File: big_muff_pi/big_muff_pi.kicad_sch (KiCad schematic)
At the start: 77 parts, among them J1 Jack_6.35, J2 Jack_6.35, J6 top_panel_connector, J7 Conn_01x01_Socket, J8 Conn_01x01_Socket, J9 Barrel_Jack_Switch, P1 front_panel, P2 bottom_panel, Q1 MMBT5551, Q10 AO3401A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

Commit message: small mods.
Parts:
- removed SIM1: Logo_Open_Hardware_Small, Symbol:OSHW-Logo2_7.3x6mm_SilkScreen, symbol Graphic:Logo_Open_Hardware_Small
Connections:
- net 0: now also J6.16 (Pin_16); no longer J6.6 (Pin_6)
- net FS_OUT: now also J6.2 (Pin_2); no longer J6.12 (Pin_12)
- net at J6.4 (Pin_4): now also R7.1; no longer SW1.3 (C)
- net at C11.2: now also J6.12 (Pin_12); no longer J6.2 (Pin_2)
- net at J6.14 (Pin_14): now also SW1.3 (C); no longer R7.1
- net at R6.1: now also J6.6 (Pin_6); no longer J6.16 (Pin_16)
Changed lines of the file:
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@@
 	)
 	(symbol
+		(lib_id "pedale:top_panel_connector")
+		(at 134.62 54.61 0)
+		(unit 1)
+		(exclude_from_sim no)
+		(in_bom yes)
+		(on_board yes)
+		(dnp no)
+		(property "Reference" "J6"
+			(at 135.636 46.228 0)
+			(effects
+				(font
+					(size 1.27 1.27)
+				)
+				(hide yes)
+			)
+		)
+		(property "Value" "top_panel_connector"
+			(at 137.16 59.69 0)
+			(effects
+				(font
+					(size 1.27 1.27)
+				)
+				(hide yes)
+			)
+		)
+		(property "Footprint" "Connector_IDC:IDC-Header_2x08_P2.54mm_Vertical"
+			(at 134.62 54.61 0)
+			(effects
+				(font
+					(size 1.27 1.27)
+				)
+				(hide yes)
+			)
+		)
+		(property "Datasheet" "~"
+			(at 134.62 54.61 0)
+			(effects
+				(font
+					(size 1.27 1.27)
+				)
+				(hide yes)
+			)
+		)
+		(property "Description" ""
+			(at 120.65 94.234 0)
+			(effects
+				(font
+					(size 1.27 1.27)
+				)
+				(hide yes)
+			)
+		)
+		(pin "8"
+		)
+		(pin "11"
+		)
+		(pin "13"
+		)
+		(pin "9"
+		)
+		(pin "16"
+		)
+		(pin "14"
+		)
+		(pin "15"
+		)
+		(pin "1"
+		)
+		(pin "10"
+		)
+		(pin "3"
+		)
+		(pin "7"
+		)
+		(pin "2"
+		)
+		(pin "5"
+		)
+		(pin "4"
+		)
+		(pin "6"
+		)
+		(pin "12"
+		)
+		(instances
+			(project "big_muff_pi"
+				(path "/1fda0e48-ac05-4486-b24b-352a2425b266"
+					(reference "J6")
+					(unit 1)
+				)
+			)
+		)
+	)
+	(symbol
 		(lib_id "Simulation_SPICE:0")
 		(at 54.61 143.51 0)
@@
 	)
 	(symbol
-		(lib_id "Graphic:Logo_Open_Hardware_Small")
-		(at 77.47 91.44 0)
-		(unit 1)
-		(exclude_from_sim no)
-		(in_bom yes)
-		(on_board yes)
-		(dnp no)
-		(fields_autoplaced yes)
-		(property "Reference" "SIM1"
-			(at 77.47 84.455 0)
-			(effects
-				(font
-					(size 1.27 1.27)
-				)
-				(hide yes)
-			)
-		)
-		(property "Value" "Logo_Open_Hardware_Small"
-			(at 77.47 97.155 0)
-			(effects
-				(font
-					(size 1.27 1.27)
-				)
-				(hide yes)
-			)
-		)
-		(property "Footprint" "Symbol:OSHW-Logo2_7.3x6mm_SilkScreen"
-			(at 77.47 91.44 0)
-			(effects
-				(font
-					(size 1.27 1.27)
-				)
-				(hide yes)
-			)
-		)
-		(property "Datasheet" "~"
-			(at 77.47 91.44 0)
-			(effects
-				(font
-					(size 1.27 1.27)
-				)
-				(hide yes)
-			)
-		)
-		(property "Description" "Open Hardware logo, small"
-			(at 77.47 91.44 0)
-			(effects
-				(font
-					(size 1.27 1.27)
-				)
-				(hide yes)
-			)
-		)
-		(instances
-			(project ""
-				(path "/1fda0e48-ac05-4486-b24b-352a2425b266"
-					(reference "SIM1")
-					(unit 1)
-				)
-			)
-		)
-	)
-	(symbol
 		(lib_id "Device:R")
 		(at 130.81 167.64 0)
@@
 	)
 	(symbol
-		(lib_id "pedale:top_panel_connector")
-		(at 172.72 125.73 0)
-		(unit 1)
-		(exclude_from_sim no)
-		(in_bom yes)
-		(on_board yes)
-		(dnp no)
-		(property "Reference" "J6"
-			(at 173.736 117.348 0)
-			(effects
-				(font
-					(size 1.27 1.27)
-				)
-				(hide yes)
-			)
-		)
-		(property "Value" "top_panel_connector"
-			(at 175.26 130.81 0)
-			(effects
-				(font
-					(size 1.27 1.27)
-				)
-				(hide yes)
-			)
-		)
-		(property "Footprint" "Connector_IDC:IDC-Header_2x08_P2.54mm_Vertical"
-			(at 172.72 125.73 0)
-			(effects
-				(font
-					(size 1.27 1.27)
-				)
-				(hide yes)
-			)
-		)
-		(property "Datasheet" "~"
-			(at 172.72 125.73 0)
-			(effects
-				(font
-					(size 1.27 1.27)
-				)
-				(hide yes)
-			)
-		)
-		(property "Description" ""
-			(at 158.75 165.354 0)
-			(effects
-				(font
-					(size 1.27 1.27)
-				)
-				(hide yes)
-			)
-		)
-		(pin "8"
-		)
-		(pin "11"
-		)
-		(pin "13"
-		)
-		(pin "9"
-		)
-		(pin "16"
-		)
-		(pin "14"
-		)
-		(pin "15"
-		)
-		(pin "1"
-		)
-		(pin "10"
-		)
-		(pin "3"
-		)
-		(pin "7"
-		)
-		(pin "2"
-		)
-		(pin "5"
-		)
-		(pin "4"
-		)
-		(pin "6"
-		)
-		(pin "12"
-		)
-		(instances
-			(project "big_muff_pi"
-				(path "/1fda0e48-ac05-4486-b24b-352a2425b266"
-					(reference "J6")
-					(unit 1)
-				)
-			)
-		)
-	)
-	(symbol
-		(lib_id "pedale:top_panel_connector")
-		(at 134.62 54.61 0)
-		(unit 3)
-		(exclude_from_sim no)
-		(in_bom yes)
-		(on_board yes)
-		(dnp no)
-		(fields_autoplaced yes)
-		(property "Reference" "J6"
-			(at 135.636 46.228 0)
-			(effects
-				(font
-					(size 1.27 1.27)
-				)
-				(hide yes)
-			)
-		)
-		(property "Value" "top_panel_connector"
-			(at 137.16 59.69 0)
-			(effects
-				(font
-					(size 1.27 1.27)
-				)
-				(hide yes)
-			)
-		)
-		(property "Footprint" "Connector_IDC:IDC-Header_2x08_P2.54mm_Vertical"
-			(at 134.62 54.61 0)
-			(effects
-				(font
-					(size 1.27 1.27)
-				)
-				(hide yes)
-			)
-		)
-		(property "Datasheet" "~"
-			(at 134.62 54.61 0)
-			(effects
-				(font
-					(size 1.27 1.27)
-				)
-				(hide yes)
-			)
-		)
-		(property "Description" ""
-			(at 120.65 94.234 0)
-			(effects
-				(font
-					(size 1.27 1.27)
-				)
-				(hide yes)
-			)
-		)
-		(pin "8"
-		)
-		(pin "11"
-		)
-		(pin "13"
-		)
-		(pin "9"
-		)
-		(pin "16"
-		)
-		(pin "14"
-		)
-		(pin "15"
-		)
-		(pin "1"
-		)
-		(pin "10"
-		)
-		(pin "3"
-		)
-		(pin "7"
-		)
-		(pin "2"
-		)
-		(pin "5"
-		)
-		(pin "4"
-		)
-		(pin "6"
-		)
-		(pin "12"
-		)
-		(instances
-			(project "big_muff_pi"
-				(path "/1fda0e48-ac05-4486-b24b-352a2425b266"
-					(reference "J6")
-					(unit 3)
-				)
-			)
-		)
-	)
-	(symbol
 		(lib_id "Transistor_BJT:BC817")
 		(at 229.87 55.88 0)
@@
 				)
 			)
+		)
+	)
+	(symbol
+		(lib_id "pedale:top_panel_connector")
+		(at 172.72 125.73 0)
+		(unit 3)
+		(exclude_from_sim no)
+		(in_bom yes)
+		(on_board yes)
+		(dnp no)
+		(property "Reference" "J6"
+			(at 173.736 117.348 0)
+			(effects
+				(font
+					(size 1.27 1.27)
+				)
+				(hide yes)
+			)
+		)
+		(property "Value" "top_panel_connector"
+			(at 175.26 130.81 0)
+			(effects
+				(font
+					(size 1.27 1.27)
+				)
+				(hide yes)
+			)
+		)
+		(property "Footprint" "Connector_IDC:IDC-Header_2x08_P2.54mm_Vertical"
+			(at 172.72 125.73 0)
+			(effects
+				(font
+					(size 1.27 1.27)
+				)
+				(hide yes)
+			)
+		)
+		(property "Datasheet" "~"
+			(at 172.72 125.73 0)
+			(effects
+				(font
+					(size 1.27 1.27)
+				)
+				(hide yes)
+			)
+		)
+		(property "Description" ""
+			(at 158.75 165.354 0)
+			(effects
+				(font
+					(size 1.27 1.27)
+				)
+				(hide yes)
+			)
+		)
+		(pin "8"
+		)
+		(pin "11"
+		)
+		(pin "13"
+		)
+		(pin "9"
+		)
+		(pin "16"
+		)
+		(pin "14"
+		)
+		(pin "15"
+		)
+		(pin "1"
+		)
+		(pin "10"
+		)
+		(pin "3"
+		)
+		(pin "7"
+		)
+		(pin "2"
+		)
+		(pin "5"
+		)
+		(pin "4"
+		)
+		(pin "6"
+		)
+		(pin "12"
+		)
+		(instances
+			(project "big_muff_pi"
+				(path "/1fda0e48-ac05-4486-b24b-352a2425b266"
+					(reference "J6")
+					(unit 3)
+				)
+			)

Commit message: New switch, fixed courtyards.
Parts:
- SW1: footprint pedale:foot_switch_tht_and_floating -> pedale:foot_switch_tht_no_pad
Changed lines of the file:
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@@
 			)
 		)
-		(property "Footprint" "pedale:foot_switch_tht_and_floating"
+		(property "Footprint" "pedale:foot_switch_tht_no_pad"
 			(at 260.35 114.3 0)
 			(effects
@@
 			)
 		)
-		(property "Footprint" "pedale:foot_switch_tht_and_floating"
+		(property "Footprint" "pedale:foot_switch_tht_no_pad"
 			(at 204.47 128.27 0)
 			(effects

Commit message: Main board almost ready.
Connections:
- no-connect marks 4 -> 11
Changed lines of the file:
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@@
+	)
+	(no_connect
+		(at 30.48 54.61)
+	)
+	(no_connect
+		(at 218.44 125.73)
 	)
 	(no_connect
@@
 	)
 	(no_connect
+		(at 218.44 135.89)
+	)
+	(no_connect
 		(at 182.88 154.94)
+	)
+	(no_connect
+		(at 30.48 57.15)
 	)
 	(no_connect
@@
 		(at 182.88 160.02)
 	)
+	(no_connect
+		(at 30.48 49.53)
+	)
+	(no_connect
+		(at 218.44 130.81)
+	)
+	(no_connect
+		(at 218.44 133.35)
+	)
 	(wire

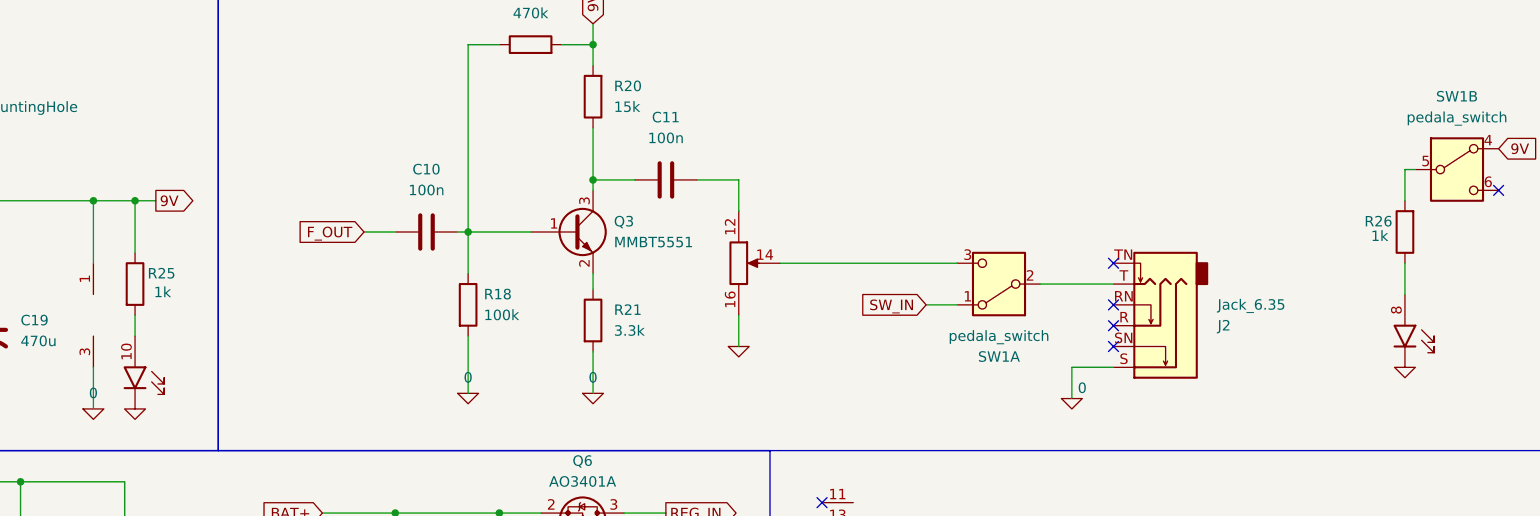
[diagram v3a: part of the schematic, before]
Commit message: 2.2k LED.
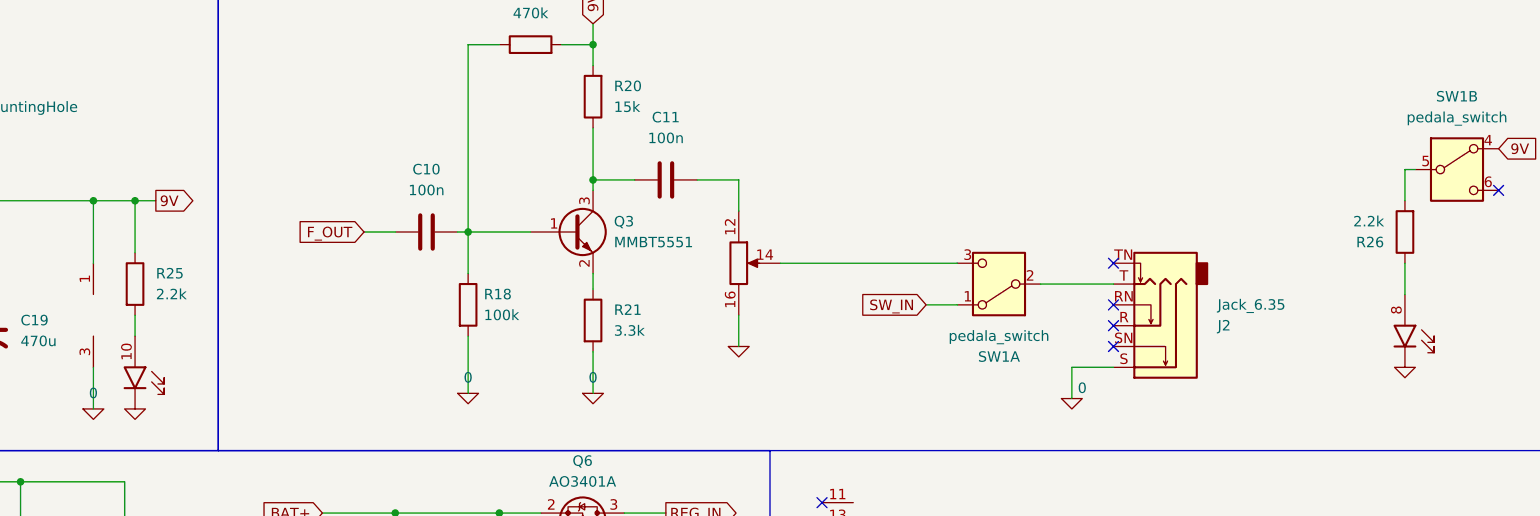
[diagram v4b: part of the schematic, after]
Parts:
- R25, R26: value 1k -> 2.2k; LCSC C21190 -> C4190
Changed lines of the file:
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@@
-	(symbol
-		(lib_id "Device:R")
-		(at 99.06 128.27 0)
-		(unit 1)
-		(exclude_from_sim no)
-		(in_bom yes)
-		(on_board yes)
-		(dnp no)
-		(property "Reference" "R25"
-			(at 100.584 127 0)
-			(effects
-				(font
-					(size 1.27 1.27)
-				)
-				(justify left)
-			)
-		)
-		(property "Value" "1k"
-			(at 101.346 129.286 0)
-			(effects
-				(font
-					(size 1.27 1.27)
-				)
-				(justify left)
-			)
-		)
-		(property "Footprint" "Resistor_SMD:R_0603_1608Metric_Pad0.98x0.95mm_HandSolder"
-			(at 97.282 128.27 90)
-			(effects
-				(font
-					(size 1.27 1.27)
-				)
-				(hide yes)
-			)
-		)
-		(property "Datasheet" "~"
-			(at 99.06 128.27 0)
-			(effects
-				(font
-					(size 1.27 1.27)
-				)
-				(hide yes)
-			)
-		)
-		(property "Description" ""
-			(at 99.06 128.27 0)
-			(effects
-				(font
-					(size 1.27 1.27)
-				)
-			)
-		)
-		(property "LCSC" "C21190"
-			(at 99.06 128.27 90)
-			(effects
-				(font
-					(size 1.27 1.27)
-				)
-				(hide yes)
-			)
-		)
-		(pin "1"
-		)
-		(pin "2"
-		)
-		(instances
-			(project "big_muff_pi"
-				(path "/1fda0e48-ac05-4486-b24b-352a2425b266"
-					(reference "R25")
-					(unit 1)
-				)
-			)
-		)
-	)
 	(symbol
 		(lib_id "Device:R")
@@
 	(symbol
 		(lib_id "Device:R")
+		(at 99.06 128.27 0)
+		(unit 1)
+		(exclude_from_sim no)
+		(in_bom yes)
+		(on_board yes)
+		(dnp no)
+		(property "Reference" "R25"
+			(at 101.6 126.9999 0)
+			(effects
+				(font
+					(size 1.27 1.27)
+				)
+				(justify left)
+			)
+		)
+		(property "Value" "2.2k"
+			(at 101.6 129.5399 0)
+			(effects
+				(font
+					(size 1.27 1.27)
+				)
+				(justify left)
+			)
+		)
+		(property "Footprint" "Resistor_SMD:R_0603_1608Metric_Pad0.98x0.95mm_HandSolder"
+			(at 97.282 128.27 90)
+			(effects
+				(font
+					(size 1.27 1.27)
+				)
+				(hide yes)
+			)
+		)
+		(property "Datasheet" "~"
+			(at 99.06 128.27 0)
+			(effects
+				(font
+					(size 1.27 1.27)
+				)
+				(hide yes)
+			)
+		)
+		(property "Description" ""
+			(at 99.06 128.27 0)
+			(effects
+				(font
+					(size 1.27 1.27)
+				)
+			)
+		)
+		(property "LCSC" "C4190"
+			(at 99.06 128.27 90)
+			(effects
+				(font
+					(size 1.27 1.27)
+				)
+				(hide yes)
+			)
+		)
+		(pin "1"
+		)
+		(pin "2"
+		)
+		(instances
+			(project "big_muff_pi"
+				(path "/1fda0e48-ac05-4486-b24b-352a2425b266"
+					(reference "R25")
+					(unit 1)
+				)
+			)
+		)
+	)
+	(symbol
+		(lib_id "Device:R")
 		(at 190.5 17.78 270)
 		(mirror x)
@@
 	)
 	(symbol
+		(lib_id "Device:R")
+		(at 254 121.92 180)
+		(unit 1)
+		(exclude_from_sim no)
+		(in_bom yes)
+		(on_board yes)
+		(dnp no)
+		(property "Reference" "R26"
+			(at 251.46 123.1901 0)
+			(effects
+				(font
+					(size 1.27 1.27)
+				)
+				(justify left)
+			)
+		)
+		(property "Value" "2.2k"
+			(at 251.46 120.6501 0)
+			(effects
+				(font
+					(size 1.27 1.27)
+				)
+				(justify left)
+			)
+		)
+		(property "Footprint" "Resistor_SMD:R_0603_1608Metric_Pad0.98x0.95mm_HandSolder"
+			(at 255.778 121.92 90)
+			(effects
+				(font
+					(size 1.27 1.27)
+				)
+				(hide yes)
+			)
+		)
+		(property "Datasheet" "~"
+			(at 254 121.92 0)
+			(effects
+				(font
+					(size 1.27 1.27)
+				)
+				(hide yes)
+			)
+		)
+		(property "Description" ""
+			(at 254 121.92 0)
+			(effects
+				(font
+					(size 1.27 1.27)
+				)
+			)
+		)
+		(property "LCSC" "C4190"
+			(at 254 121.92 90)
+			(effects
+				(font
+					(size 1.27 1.27)
+				)
+				(hide yes)
+			)
+		)
+		(pin "1"
+		)
+		(pin "2"
+		)
+		(instances
+			(project "big_muff_pi"
+				(path "/1fda0e48-ac05-4486-b24b-352a2425b266"
+					(reference "R26")
+					(unit 1)
+				)
+			)
+		)
+	)
+	(symbol
 		(lib_id "Device:C")
 		(at 219.71 27.94 90)
@@
 					(unit 1)
 				)
-			)
-		)
-	)
-	(symbol
-		(lib_id "Device:R")
-		(at 254 121.92 180)
-		(unit 1)
-		(exclude_from_sim no)
-		(in_bom yes)
-		(on_board yes)
-		(dnp no)
-		(property "Reference" "R26"
-			(at 252.476 120.65 0)
-			(effects
-				(font
-					(size 1.27 1.27)
-				)
-				(justify left)
-			)
-		)
-		(property "Value" "1k"
-			(at 251.968 122.428 0)
-			(effects
-				(font
-					(size 1.27 1.27)
-				)
-				(justify left)
-			)
-		)
-		(property "Footprint" "Resistor_SMD:R_0603_1608Metric_Pad0.98x0.95mm_HandSolder"
-			(at 255.778 121.92 90)
-			(effects
-				(font
-					(size 1.27 1.27)
-				)
-				(hide yes)
-			)
-		)
-		(property "Datasheet" "~"
-			(at 254 121.92 0)
-			(effects
-				(font
-					(size 1.27 1.27)
-				)
-				(hide yes)
-			)
-		)
-		(property "Description" ""
-			(at 254 121.92 0)
-			(effects
-				(font
-					(size 1.27 1.27)
-				)
-			)
-		)
-		(property "LCSC" "C21190"
-			(at 254 121.92 90)
-			(effects
-				(font
-					(size 1.27 1.27)
-				)
-				(hide yes)
-			)
-		)
-		(pin "1"
-		)
-		(pin "2"
-		)
-		(instances
-			(project "big_muff_pi"
-				(path "/1fda0e48-ac05-4486-b24b-352a2425b266"
-					(reference "R26")
-					(unit 1)
-				)

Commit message: dfasdf dfasdf
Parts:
- J6: footprint Connector_IDC:IDC-Header_2x08_P2.54mm_Vertical -> pedale:IDC-Header_2x08_P2.54mm_Vertical
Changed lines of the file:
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@@
 			)
 		)
-		(property "Footprint" "Connector_IDC:IDC-Header_2x08_P2.54mm_Vertical"
+		(property "Footprint" "pedale:IDC-Header_2x08_P2.54mm_Vertical"
 			(at 134.62 54.61 0)
 			(effects
@@
 			)
 		)
-		(property "Footprint" "Connector_IDC:IDC-Header_2x08_P2.54mm_Vertical"
+		(property "Footprint" "pedale:IDC-Header_2x08_P2.54mm_Vertical"
 			(at 182.88 160.02 0)
 			(effects
@@
 			)
 		)
-		(property "Footprint" "Connector_IDC:IDC-Header_2x08_P2.54mm_Vertical"
+		(property "Footprint" "pedale:IDC-Header_2x08_P2.54mm_Vertical"
 			(at 264.16 53.34 0)
 			(effects
@@
 			)
 		)
-		(property "Footprint" "Connector_IDC:IDC-Header_2x08_P2.54mm_Vertical"
+		(property "Footprint" "pedale:IDC-Header_2x08_P2.54mm_Vertical"
 			(at 93.98 138.43 0)
 			(effects
@@
 			)
 		)
-		(property "Footprint" "Connector_IDC:IDC-Header_2x08_P2.54mm_Vertical"
+		(property "Footprint" "pedale:IDC-Header_2x08_P2.54mm_Vertical"
 			(at 254 134.62 0)
 			(effects
@@
 			)
 		)
-		(property "Footprint" "Connector_IDC:IDC-Header_2x08_P2.54mm_Vertical"
+		(property "Footprint" "pedale:IDC-Header_2x08_P2.54mm_Vertical"
 			(at 99.06 139.7 0)
 			(effects
@@
 			)
 		)
-		(property "Footprint" "Connector_IDC:IDC-Header_2x08_P2.54mm_Vertical"
+		(property "Footprint" "pedale:IDC-Header_2x08_P2.54mm_Vertical"
 			(at 172.72 125.73 0)
 			(effects
